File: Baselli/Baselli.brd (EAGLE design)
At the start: 54 x 54 mm, 91 parts, among them J1 FTDI-SER-6-PP, J4 JTAG_PROG, Q1 8MHz NP, Q2 IRLML2244, SW1 A6H-2101, U1 STM32F051R8T, U4 LCMXO2-256HC-4SG32, X1 M-BOLT-2, X2 M-BOLT-2, X3 M-BOLT-2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

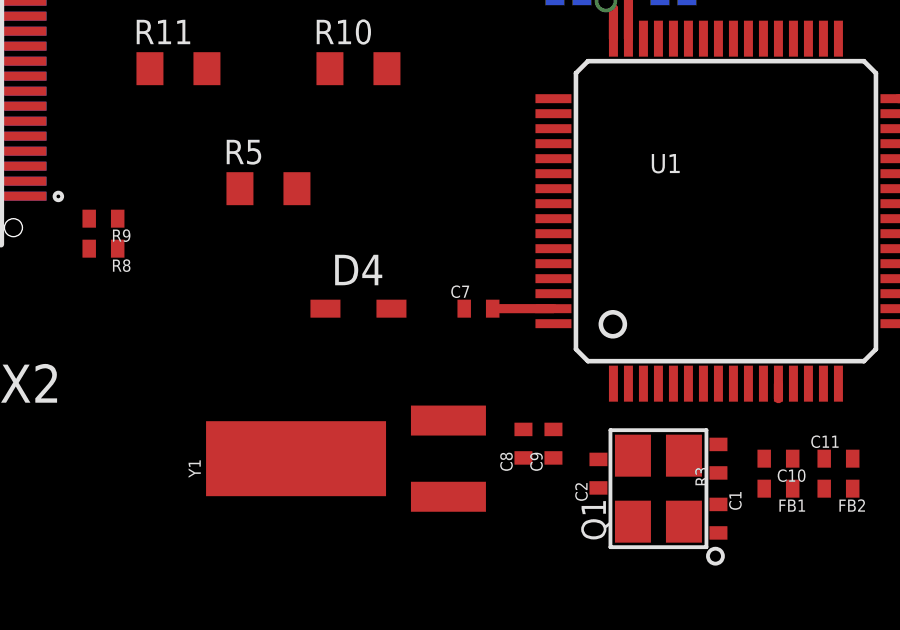
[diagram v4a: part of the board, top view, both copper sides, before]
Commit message: Changed wire classes in Baselli
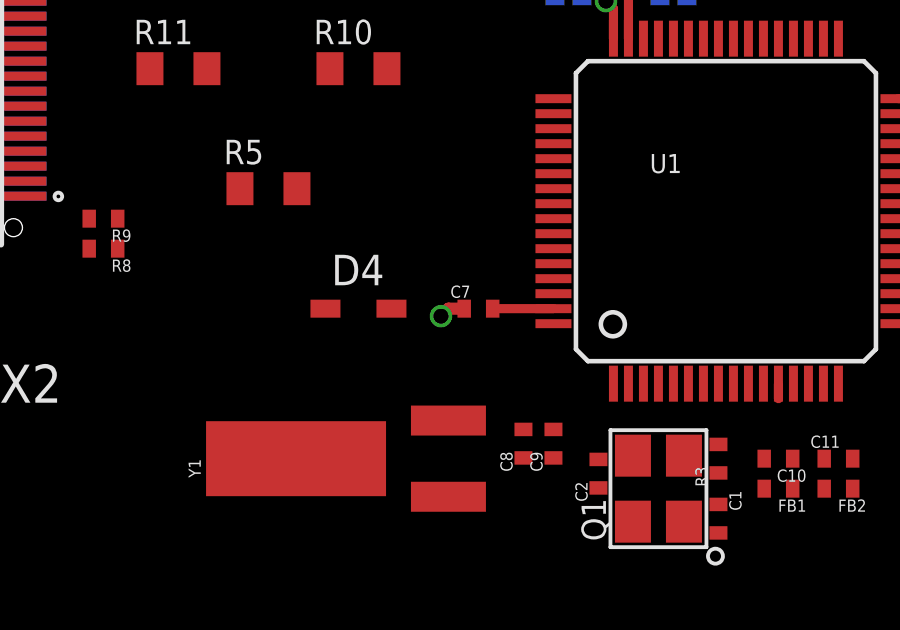
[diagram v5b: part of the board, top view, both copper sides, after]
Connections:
- net N$1 renamed VCCIO0
- net N$2 renamed VCCIO1
- net N$3 renamed VCCIO2
- net N$4 renamed VCCIO3
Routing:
- net +3V3: track 10.8 -> 11.7 mm, vias 3 -> 4
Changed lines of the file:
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@@
 <layers>
 <layer number="1" name="Top" color="4" fill="1" visible="yes" active="yes"/>
-<layer number="2" name="Layer2" color="1" fill="9" visible="yes" active="yes"/>
+<layer number="2" name="Layer2" color="1" fill="9" visible="no" active="yes"/>
 <layer number="3" name="Route3" color="4" fill="3" visible="no" active="no"/>
 <layer number="14" name="Route14" color="1" fill="6" visible="no" active="no"/>
-<layer number="15" name="Layer3" color="4" fill="10" visible="yes" active="yes"/>
+<layer number="15" name="Layer3" color="4" fill="10" visible="no" active="yes"/>
 <layer number="16" name="Bottom" color="1" fill="1" visible="yes" active="yes"/>
 <layer number="17" name="Pads" color="2" fill="1" visible="yes" active="yes"/>
@@
 </elements>
 <signals>
-<signal name="VDDA">
+<signal name="VDDA" class="1">
 <contactref element="C10" pad="1"/>
 <contactref element="C11" pad="1"/>
@@
 <wire x1="6.975" y1="44" x2="7.123" y2="46" width="0" layer="19" extent="1-1"/>
 </signal>
-<signal name="VSSA">
+<signal name="VSSA" class="1">
 <contactref element="C10" pad="2"/>
 <contactref element="C11" pad="2"/>
@@
 <wire x1="11.5" y1="39" x2="11.5" y2="38" width="0.3048" layer="1"/>
 <contactref element="SJ17" pad="1"/>
+<wire x1="23.525" y1="16" x2="23" y2="16" width="0.4064" layer="1"/>
+<wire x1="23" y1="16" x2="22.75" y2="15.75" width="0.4064" layer="1"/>
+<via x="22.75" y="15.75" extent="1-16" drill="0.5"/>
 <wire x1="36.0628" y1="43.75" x2="35.37" y2="45.83" width="0" layer="19" extent="1-16"/>
 <wire x1="36.25" y1="40.775" x2="36.0628" y2="43.75" width="0" layer="19" extent="1-16"/>
-<wire x1="26.55" y1="26.75" x2="27" y2="28.25" width="0" layer="19" extent="1-16"/>
 <wire x1="32" y1="47.475" x2="35.37" y2="45.83" width="0" layer="19" extent="1-1"/>
 <wire x1="31.545" y1="45.59" x2="32" y2="47.475" width="0" layer="19" extent="1-1"/>
 <wire x1="29.54" y1="48.6129" x2="32" y2="47.475" width="0" layer="19" extent="1-1"/>
-<wire x1="29" y1="32.5628" x2="28.025" y2="28.25" width="0" layer="19" extent="1-16"/>
-<wire x1="33.25" y1="32.475" x2="29" y2="32.5628" width="0" layer="19" extent="1-16"/>
+<wire x1="33.5" y1="34" x2="36" y2="39" width="0" layer="19" extent="1-1"/>
+<wire x1="29" y1="32.5628" x2="33.25" y2="32.475" width="0" layer="19" extent="1-16"/>
+<wire x1="28.025" y1="28.25" x2="29" y2="32.5628" width="0" layer="19" extent="1-16"/>
+<wire x1="26.55" y1="26.75" x2="27" y2="28.25" width="0" layer="19" extent="1-16"/>
 <wire x1="27" y1="36.5628" x2="29" y2="32.5628" width="0" layer="19" extent="16-16"/>
-<wire x1="47.35" y1="17.5" x2="52" y2="17" width="0" layer="19" extent="1-1"/>
-<wire x1="41" y1="18.475" x2="47.35" y2="17.5" width="0" layer="19" extent="1-1"/>
-<wire x1="40.45" y1="20" x2="41" y2="18.475" width="0" layer="19" extent="1-16"/>
-<wire x1="40.025" y1="23" x2="40.45" y2="20" width="0" layer="19" extent="1-16"/>
-<wire x1="8.877" y1="46" x2="10.475" y2="39" width="0" layer="19" extent="1-1"/>
 <wire x1="40.5" y1="30.9372" x2="33.5" y2="33.225" width="0" layer="19" extent="1-16"/>
+<wire x1="40.025" y1="23" x2="40.5" y2="30.9372" width="0" layer="19" extent="1-16"/>
+<wire x1="40.45" y1="20" x2="40.025" y2="23" width="0" layer="19" extent="1-16"/>
+<wire x1="41" y1="18.475" x2="40.45" y2="20" width="0" layer="19" extent="1-16"/>
+<wire x1="47.35" y1="17.5" x2="41" y2="18.475" width="0" layer="19" extent="1-1"/>
+<wire x1="52" y1="17" x2="47.35" y2="17.5" width="0" layer="19" extent="1-1"/>
 <wire x1="49" y1="30.85" x2="40.5" y2="30.9372" width="0" layer="19" extent="1-16"/>
-<wire x1="5.1999" y1="31.25" x2="10.475" y2="38" width="0" layer="19" extent="1-1"/>
-<wire x1="5.1999" y1="31.25" x2="5.1999" y2="31.25" width="0" layer="19" extent="1-16"/>
-<wire x1="5.1999" y1="29.75" x2="5.1999" y2="31.25" width="0" layer="19" extent="1-1"/>
-<wire x1="5.1999" y1="29.75" x2="5.1999" y2="29.75" width="0" layer="19" extent="1-16"/>
-<wire x1="2" y1="29.775" x2="5.1999" y2="29.75" width="0" layer="19" extent="1-1"/>
-<wire x1="5.1999" y1="20.75" x2="5.1999" y2="29.75" width="0" layer="19" extent="1-16"/>
-<wire x1="5.1999" y1="20.75" x2="5.1999" y2="20.75" width="0" layer="19" extent="1-16"/>
-<wire x1="11.975" y1="19" x2="5.1999" y2="20.75" width="0" layer="19" extent="1-16"/>
-<wire x1="11.975" y1="18" x2="11.975" y2="19" width="0" layer="19" extent="1-1"/>
 <wire x1="23.525" y1="16" x2="26.55" y2="26.75" width="0" layer="19" extent="1-16"/>
 <wire x1="26.5" y1="15.5" x2="23.525" y2="16" width="0" layer="19" extent="1-1"/>
 <wire x1="33.525" y1="10" x2="26.5" y2="15.5" width="0" layer="19" extent="1-1"/>
+<wire x1="11.975" y1="18" x2="22.75" y2="15.75" width="0" layer="19" extent="1-1"/>
+<wire x1="11.975" y1="19" x2="11.975" y2="18" width="0" layer="19" extent="1-1"/>
+<wire x1="5.1999" y1="20.75" x2="11.975" y2="19" width="0" layer="19" extent="1-16"/>
+<wire x1="5.1999" y1="20.75" x2="5.1999" y2="20.75" width="0" layer="19" extent="1-16"/>
+<wire x1="5.1999" y1="29.75" x2="5.1999" y2="20.75" width="0" layer="19" extent="1-16"/>
+<wire x1="5.1999" y1="29.75" x2="5.1999" y2="29.75" width="0" layer="19" extent="1-16"/>
+<wire x1="5.1999" y1="31.25" x2="5.1999" y2="29.75" width="0" layer="19" extent="1-1"/>
+<wire x1="5.1999" y1="31.25" x2="5.1999" y2="31.25" width="0" layer="19" extent="1-16"/>
+<wire x1="2" y1="29.775" x2="5.1999" y2="29.75" width="0" layer="19" extent="1-1"/>
+<wire x1="10.475" y1="38" x2="5.1999" y2="31.25" width="0" layer="19" extent="1-1"/>
+<wire x1="8.877" y1="46" x2="10.475" y2="39" width="0" layer="19" extent="1-1"/>
 </signal>
 <signal name="GNDI" class="1">
@@
 <wire x1="31" y1="30.5" x2="33" y2="30.5" width="0.4064" layer="1"/>
 <contactref element="SJ18" pad="1"/>
+<wire x1="52.5" y1="33.35" x2="52" y2="37" width="0" layer="19" extent="1-1"/>
+<wire x1="41" y1="38" x2="52" y2="37" width="0" layer="19" extent="1-1"/>
+<wire x1="36.25" y1="41.725" x2="39.975" y2="38" width="0" layer="19" extent="1-1"/>
 <wire x1="35.25" y1="41.725" x2="36.25" y2="41.725" width="0" layer="19" extent="1-1"/>
 <wire x1="32.75" y1="42" x2="35.25" y2="41.725" width="0" layer="19" extent="1-1"/>
-<wire x1="34" y1="38" x2="34" y2="37" width="0" layer="19" extent="1-1"/>
+<wire x1="34" y1="39" x2="32.75" y2="41.225" width="0" layer="19" extent="1-1"/>
+<wire x1="34" y1="37" x2="34" y2="38" width="0" layer="19" extent="1-1"/>
 <wire x1="34" y1="35" x2="34.5" y2="36.5" width="0" layer="19" extent="1-1"/>
+<wire x1="33.25" y1="31.525" x2="34" y2="34" width="0" layer="19" extent="1-1"/>
 <wire x1="30.95" y1="26.75" x2="30.25" y2="28.25" width="0" layer="19" extent="1-16"/>
+<wire x1="36" y1="31.025" x2="33.25" y2="30.75" width="0" layer="19" extent="1-1"/>
+<wire x1="30.025" y1="35.25" x2="34" y2="35" width="0" layer="19" extent="1-1"/>
 <wire x1="23" y1="33.8" x2="29.25" y2="35.25" width="0" layer="19" extent="1-1"/>
 <wire x1="38" y1="22.5" x2="37" y2="30.25" width="0" layer="19" extent="1-1"/>
@@
 <wire x1="29.5" y1="25" x2="32.25" y2="36.25" width="0" layer="19" extent="1-1"/>
 </signal>
-<signal name="PF4">
+<signal name="PF4" class="1">
 <contactref element="U1" pad="18"/>
 <contactref element="R15" pad="2"/>
@@
 <wire x1="14.95" y1="30" x2="38" y2="16" width="0" layer="19" extent="1-1"/>
 </signal>
-<signal name="PF5">
+<signal name="PF5" class="1">
 <contactref element="U1" pad="19"/>
 <contactref element="R16" pad="2"/>
@@
 <wire x1="5.1999" y1="30.25" x2="5.1999" y2="30.25" width="0" layer="19" extent="1-16"/>
 </signal>
-<signal name="VCC-IN">
+<signal name="VCC-IN" class="1">
 <contactref element="J1" pad="VCC"/>
 <contactref element="D2" pad="A"/>
@@
 <wire x1="28.27" y1="48.6129" x2="32" y2="46.525" width="0" layer="19" extent="1-1"/>
 </signal>
-<signal name="PF6">
+<signal name="PF6" class="1">
 <contactref element="U1" pad="47"/>
 <contactref element="SJ6" pad="2"/>
@@
 <wire x1="21" y1="45.95" x2="25.73" y2="48.6129" width="0" layer="19" extent="1-1"/>
 </signal>
-<signal name="PF7">
+<signal name="PF7" class="1">
 <contactref element="U1" pad="48"/>
 <contactref element="R18" pad="2"/>
@@
 <wire x1="41.4" y1="12.45" x2="38" y2="18.5" width="0" layer="19" extent="1-1"/>
 </signal>
-<signal name="VCCIO">
+<signal name="VCCIO" class="1">
 <contactref element="EXT1" pad="2"/>
 <contactref element="EXB1" pad="2"/>
@@
 <wire x1="20.475" y1="42" x2="21.992" y2="41" width="0" layer="19" extent="1-16"/>
 </signal>
-<signal name="AREF">
+<signal name="AREF" class="1">
 <contactref element="R5" pad="1"/>
 <contactref element="EXB1" pad="13"/>
@@
 <wire x1="45.5" y1="20.275" x2="47.665" y2="19.3" width="0" layer="19" extent="1-1"/>
 </signal>
-<signal name="N$2">
+<signal name="VCCIO1" class="1">
 <contactref element="U4" pad="19"/>
 <contactref element="C15" pad="1"/>
@@
 <wire x1="35.25" y1="40.775" x2="35.25" y2="43.75" width="0" layer="19" extent="1-16"/>
 </signal>
-<signal name="N$3">
+<signal name="VCCIO2" class="1">
 <contactref element="U4" pad="7"/>
 <contactref element="U4" pad="15"/>
@@
 <wire x1="40.5" y1="31.75" x2="37" y2="31.975" width="0" layer="19" extent="1-16"/>
 </signal>
-<signal name="N$4">
+<signal name="VCCIO3" class="1">
 <contactref element="U4" pad="6"/>
 <contactref element="SJ4" pad="2"/>
@@
 <wire x1="20.95" y1="27" x2="38" y2="20" width="0" layer="19" extent="1-1"/>
 </signal>
-<signal name="N$1">
+<signal name="VCCIO0" class="1">
 <contactref element="U4" pad="24"/>
 <contactref element="U4" pad="31"/>

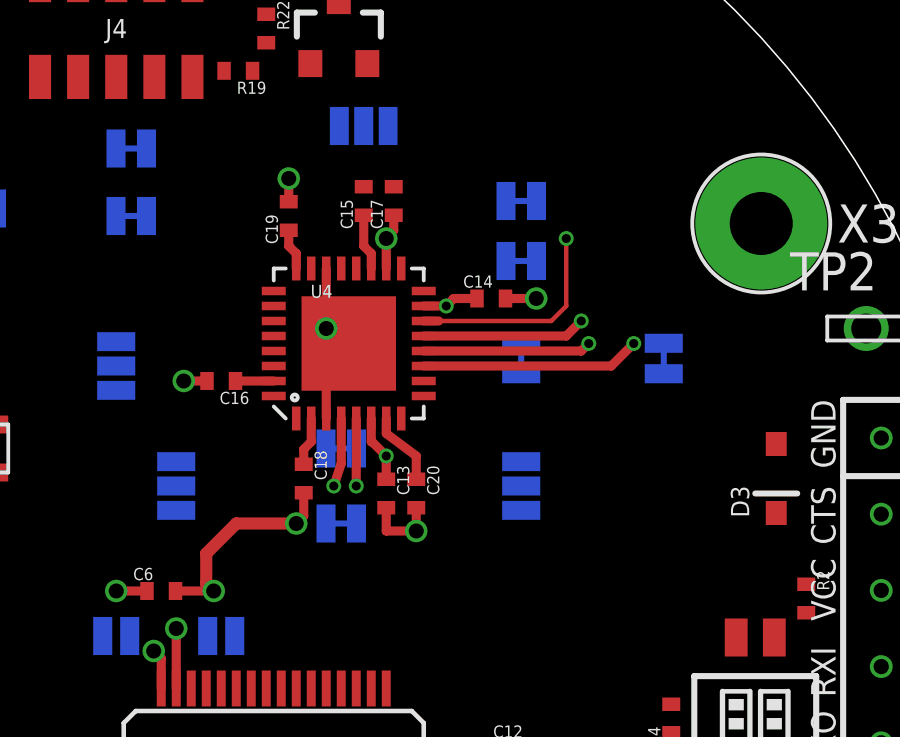
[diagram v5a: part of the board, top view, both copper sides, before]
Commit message: Tweaking Baselli, with diminsihed returns
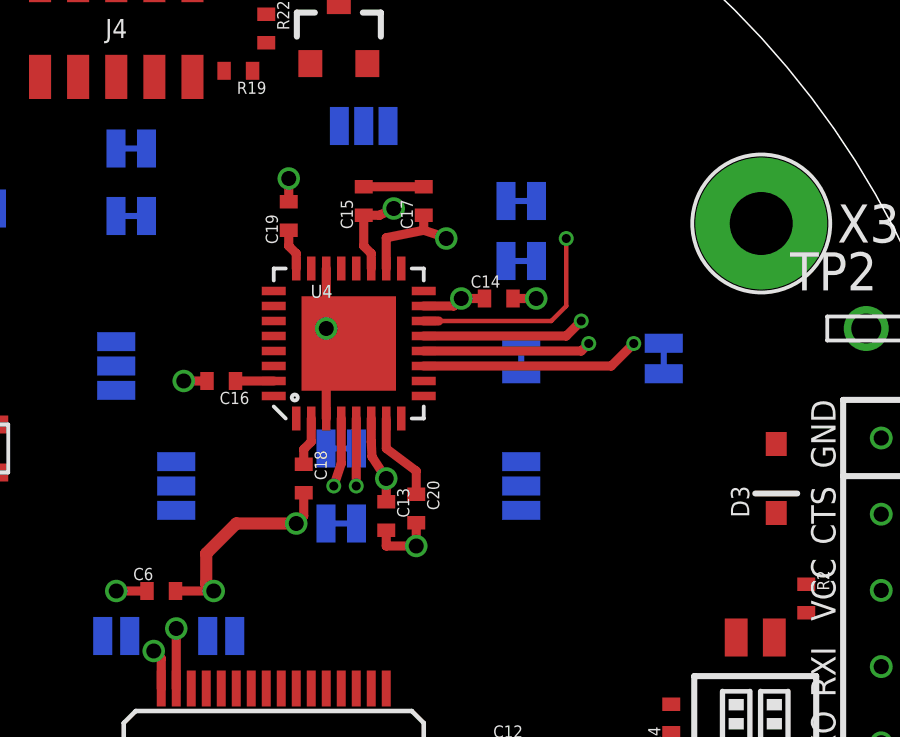
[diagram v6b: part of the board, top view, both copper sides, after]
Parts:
- moved C17 1.00 mm to (37.2, 41.2)
- moved C13 0.75 mm to (36.0, 30.8)
- moved C20 0.50 mm to (37.0, 31.0)
- moved C14 0.25 mm to (39.8, 38.0)
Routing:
- net +3V3: track 11.7 -> 13.5 mm
- net GNDI: track 17.3 -> 18.8 mm
- net VCCIO1: track 1.88 -> 2.93 mm, vias 0 -> 1
- net VCCIO2: track 4.40 -> 5.15 mm
- net VCCIO3: track 2.25 -> 2.92 mm

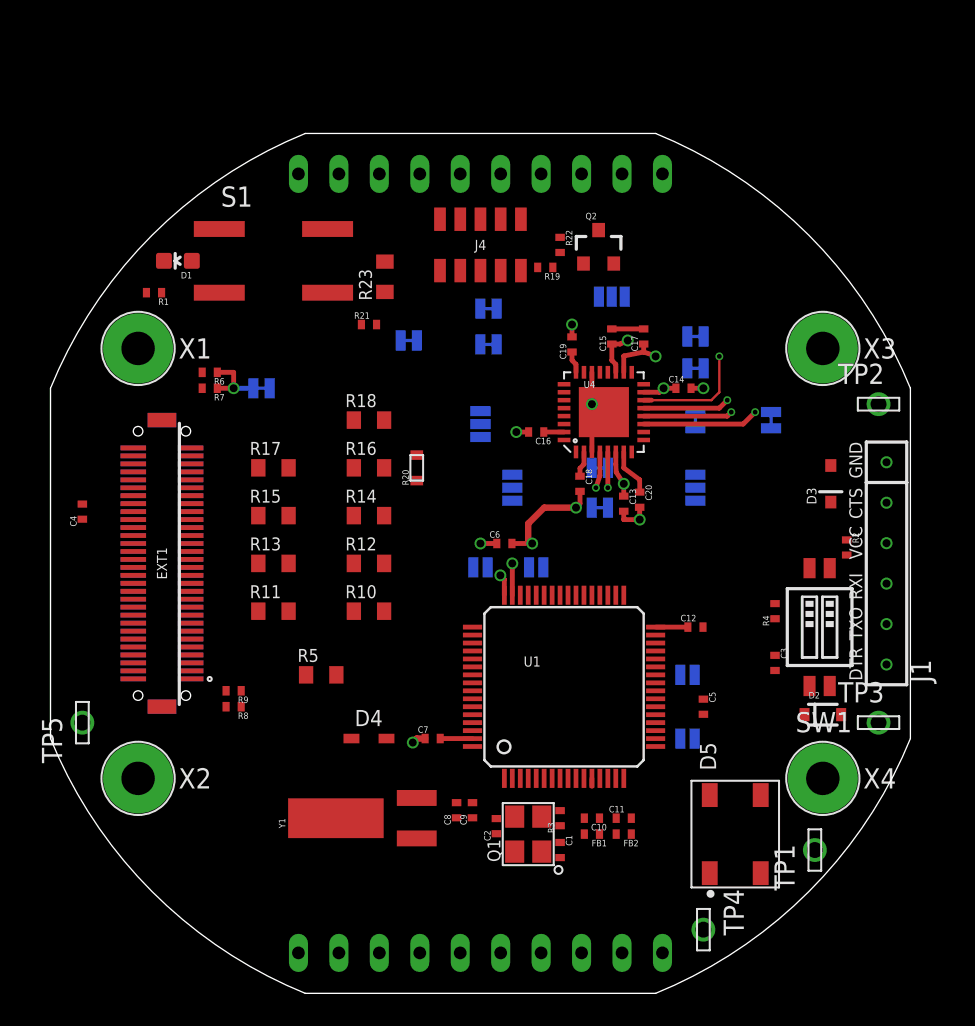
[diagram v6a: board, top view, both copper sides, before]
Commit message: Changed the LCMXO2 package to the one with vias.
Now it routes.
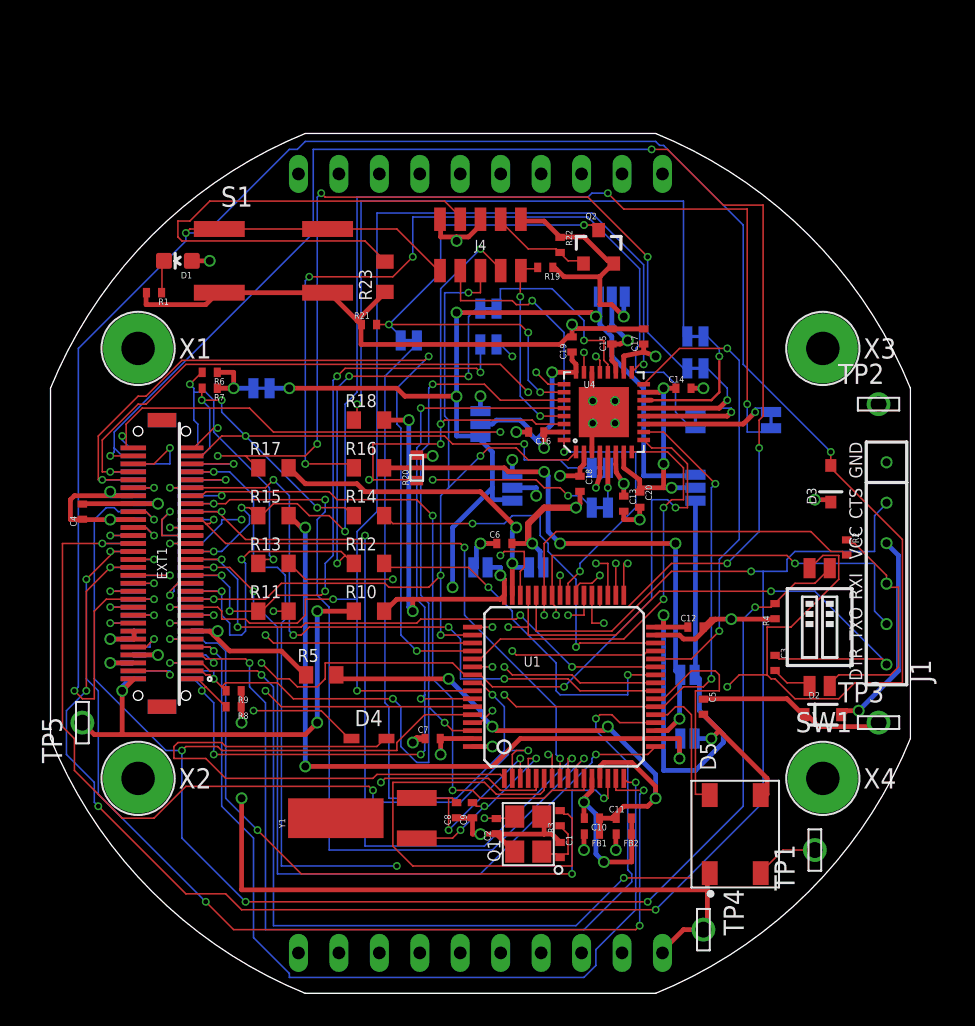
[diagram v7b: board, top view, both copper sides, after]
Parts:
- U4: value LCMXO2-256HC-4SG32 -> LCMXO2-256SG32-V; device ELL-i-DigitalIC:QFN-32 -> ELL-i-DigitalIC:QFN-32-PAD-VIAS
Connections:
- net GNDI: now also U4.VIA1, U4.VIA2, U4.VIA3, U4.VIA4
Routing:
- net NRES: track 0.00 -> 173.1 mm, vias 0 -> 6
- net D3: track 0.00 -> 111.0 mm, vias 0 -> 5
- net BOOT0: track 0.00 -> 106.4 mm, vias 0 -> 5
- net VCCIO: track 0.00 -> 97.8 mm, vias 0 -> 8
- net GNDI: track 18.8 -> 111.7 mm, vias 7 -> 15
- net E15: track 0.00 -> 90.4 mm, vias 0 -> 4
- net +3V3: track 13.5 -> 99.4 mm, vias 4 -> 17
- net D11: track 0.00 -> 78.0 mm, vias 0 -> 4
- net E0: track 0.00 -> 76.9 mm, vias 0 -> 5
- net ETH_INT: track 0.00 -> 67.9 mm, vias 0 -> 5
- net E2: track 0.00 -> 65.6 mm, vias 0 -> 5
- net E1: track 0.00 -> 65.3 mm, vias 0 -> 5
- net D4: track 0.00 -> 64.3 mm, vias 0 -> 3
- net D0: track 0.00 -> 64.2 mm, vias 0 -> 2
- net A3: track 0.00 -> 63.8 mm, vias 0 -> 3
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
